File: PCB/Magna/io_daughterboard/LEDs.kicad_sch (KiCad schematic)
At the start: 90 parts, among them U2001 74HC595, U2002 74HC595, U2003 74HC595, U2004 74HC595, U2005 74HC595

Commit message: Split schematic to several projects
To allow for several boards to be done a kicad project
is needed for each
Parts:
- added TP2001, TP2002, TP2003, TP2004, TP2005, TP2006: TestPoint, TestPoint:TestPoint_Keystone_5005-5009_Compact, symbol Connector:TestPoint
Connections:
- net SPARE_LED6 is gone; now on net SPARE_LED5: D2038.1 (K), U2005.7 (QH)
- net CH1_0db: now also R2002.2; no longer D2002.1 (K)
- net CH1_12db: now also R2006.2; no longer D2006.1 (K)
- net CH1_20db: now also R2007.2; no longer D2007.1 (K)
- net CH1_25db: now also R2008.2; no longer D2008.1 (K)
- net CH1_3db: now also R2003.2; no longer D2003.1 (K)
- net CH1_6db: now also R2004.2; no longer D2004.1 (K)
- net CH1_9db: now also R2005.2; no longer D2005.1 (K)
- net CH1_clip: now also R2001.2; no longer D2001.1 (K)
- net CH2_0db: now also R2010.2; no longer D2010.1 (K)
- net CH2_12db: now also R2014.2; no longer D2014.1 (K)
- net CH2_20db: now also R2015.2; no longer D2015.1 (K)
- net CH2_25db: now also R2016.2; no longer D2016.1 (K)
- net CH2_3db: now also R2011.2; no longer D2011.1 (K)
- net CH2_6db: now also R2012.2; no longer D2012.1 (K)
- net CH2_9db: now also R2013.2; no longer D2013.1 (K)
- net CH2_clip: now also R2009.2; no longer D2009.1 (K)
- net GND: now also TP2003.1
- net MIDI_IN_INDICATOR: now also U2005.4 (QE); no longer U2005.3 (QD)
- net Master_0db: now also R2018.2; no longer D2018.1 (K)
- net Master_12db: now also R2022.2; no longer D2022.1 (K)
- net Master_20db: now also R2023.2; no longer D2023.1 (K)
- net Master_25db: now also R2024.2; no longer D2024.1 (K)
- net Master_3db: now also R2019.2; no longer D2019.1 (K)
- net Master_6db: now also R2020.2; no longer D2020.1 (K)
- net Master_9db: now also R2021.2; no longer D2021.1 (K)
- net Master_clip: now also R2017.2; no longer D2017.1 (K)
- net OE_output_ena: now also TP2005.1
- net OE_register__CLK: now also TP2002.1
- net OE_serial_CLK: now also TP2004.1
- net OE_serial_CLR: now also TP2001.1
- net OE_serial_in: now also TP2006.1
- net SPARE_LED2: now also D2039.1 (K); no longer D2037.1 (K)
- net SPARE_LED3: now also D2040.1 (K), U2005.5 (QF); no longer D2039.1 (K), U2005.4 (QE)
- net SPARE_LED4: now also D2036.1 (K), U2005.6 (QG); no longer D2040.1 (K), U2005.5 (QF)
- net SPARE_LED5: no longer D2036.1 (K), U2005.6 (QG)
- net VDD: now also D2001.2 (A), D2002.2 (A), D2003.2 (A), D2004.2 (A), D2005.2 (A), D2006.2 (A), D2007.2 (A), D2008.2 (A), D2009.2 (A), D2010.2 (A), D2011.2 (A), D2012.2 (A), D2013.2 (A), D2014.2 (A), D2015.2 (A), D2016.2 (A), D2017.2 (A), D2018.2 (A), D2019.2 (A), D2020.2 (A), D2021.2 (A), D2022.2 (A), D2023.2 (A), D2024.2 (A); no longer R2001.2, R2002.2, R2003.2, R2004.2, R2005.2, R2006.2, R2007.2, R2008.2, R2009.2, R2010.2, R2011.2, R2012.2, R2013.2, R2014.2, R2015.2, R2016.2, R2017.2, R2018.2, R2019.2, R2020.2, R2021.2, R2022.2, R2023.2, R2024.2
- net at R2002.1: now also D2002.1 (K); no longer D2002.2 (A)
- net at R2004.1: now also D2004.1 (K); no longer D2004.2 (A)
- net at R2015.1: now also D2015.1 (K); no longer D2015.2 (A)
- net at R2005.1: now also D2005.1 (K); no longer D2005.2 (A)
- net at R2014.1: now also D2014.1 (K); no longer D2014.2 (A)
- net at R2003.1: now also D2003.1 (K); no longer D2003.2 (A)
- net at R2022.1: now also D2022.1 (K); no longer D2022.2 (A)
- net at R2019.1: now also D2019.1 (K); no longer D2019.2 (A)
- net at R2007.1: now also D2007.1 (K); no longer D2007.2 (A)
- net at R2024.1: now also D2024.1 (K); no longer D2024.2 (A)
- net at R2020.1: now also D2020.1 (K); no longer D2020.2 (A)
- net at R2023.1: now also D2023.1 (K); no longer D2023.2 (A)
- net at R2010.1: now also D2010.1 (K); no longer D2010.2 (A)
- net at R2012.1: now also D2012.1 (K); no longer D2012.2 (A)
- net at R2001.1: now also D2001.1 (K); no longer D2001.2 (A)
- net at R2018.1: now also D2018.1 (K); no longer D2018.2 (A)
- net at R2009.1: now also D2009.1 (K); no longer D2009.2 (A)
- net at R2013.1: now also D2013.1 (K); no longer D2013.2 (A)
- net at R2006.1: now also D2006.1 (K); no longer D2006.2 (A)
- net at R2017.1: now also D2017.1 (K); no longer D2017.2 (A)
- net at R2016.1: now also D2016.1 (K); no longer D2016.2 (A)
- net at R2008.1: now also D2008.1 (K); no longer D2008.2 (A)
- net at R2011.1: now also D2011.1 (K); no longer D2011.2 (A)
- net at R2021.1: now also D2021.1 (K); no longer D2021.2 (A)
- new net EFFECT_CUE_STATUS: D2037.1 (K), U2005.3 (QD)
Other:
- moved on the sheet: D2001, D2002, D2003, D2004, D2005, D2006, D2007, D2008, D2009, D2010, D2011, D2012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

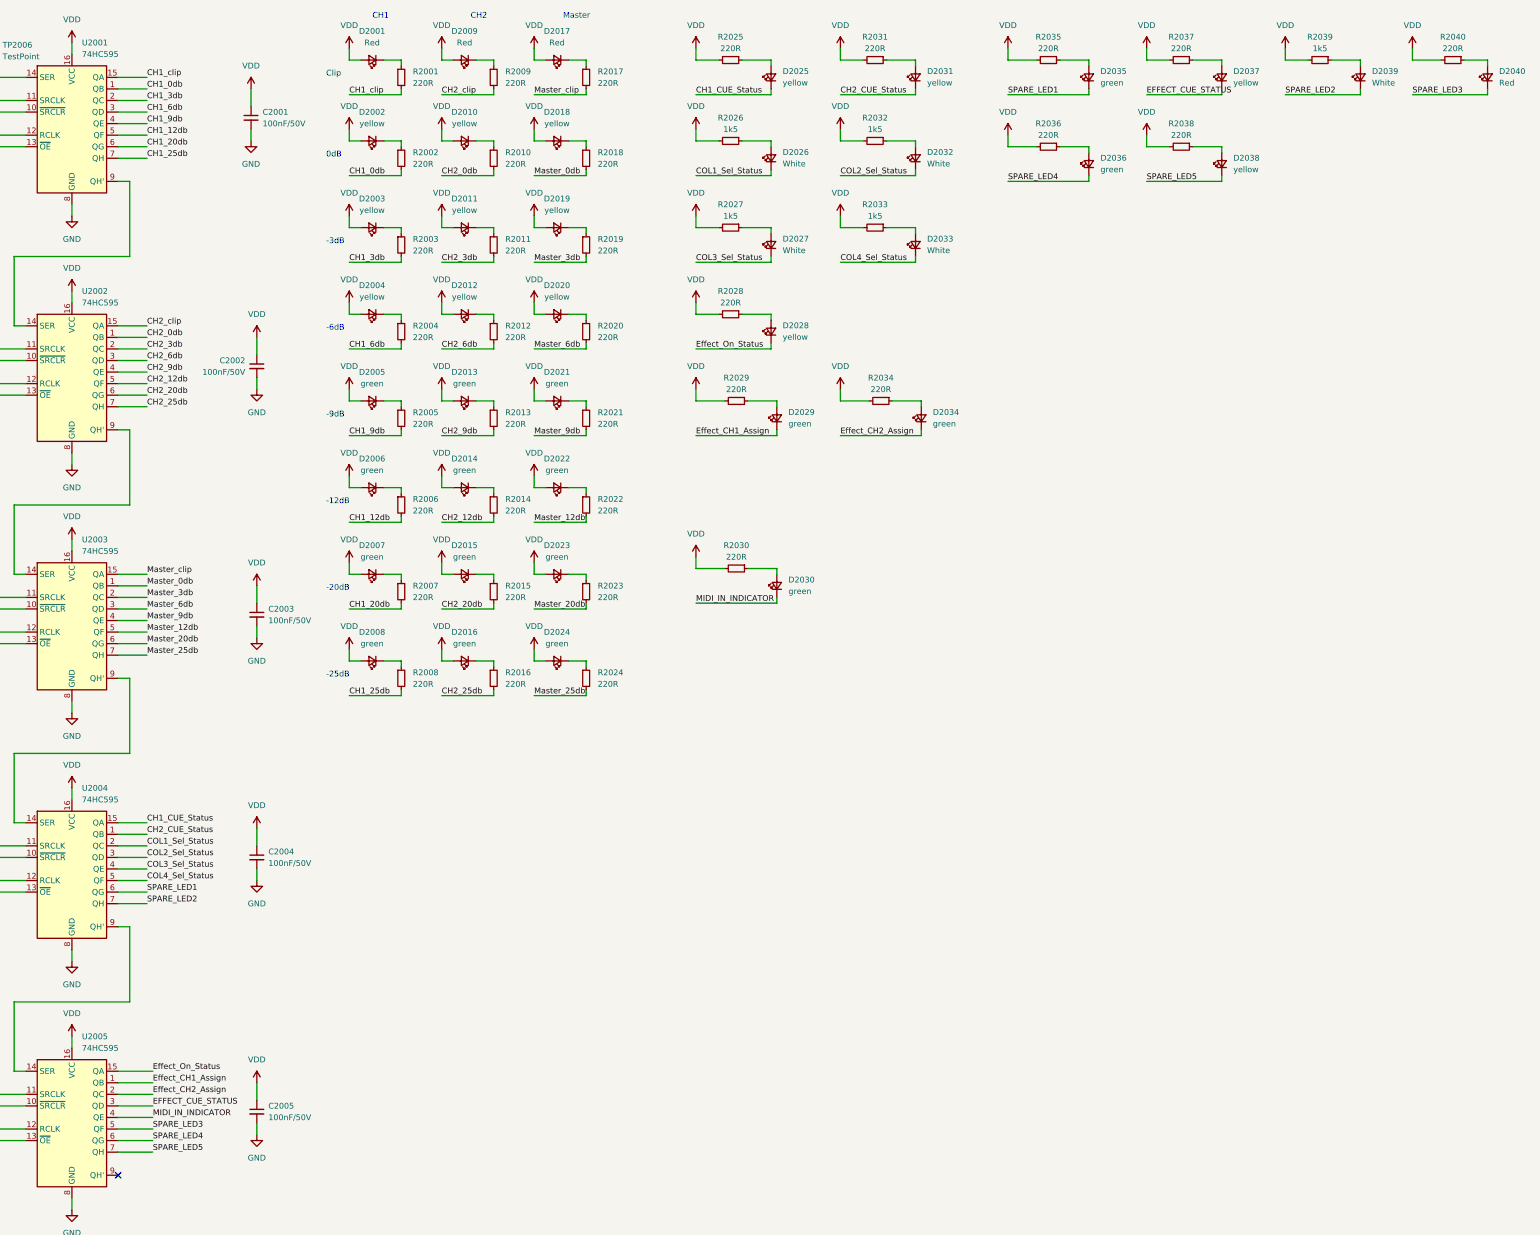
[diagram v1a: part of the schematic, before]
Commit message: Add a lot on the IO PCB
Also some schematic changes to accomodate issues found
when routing
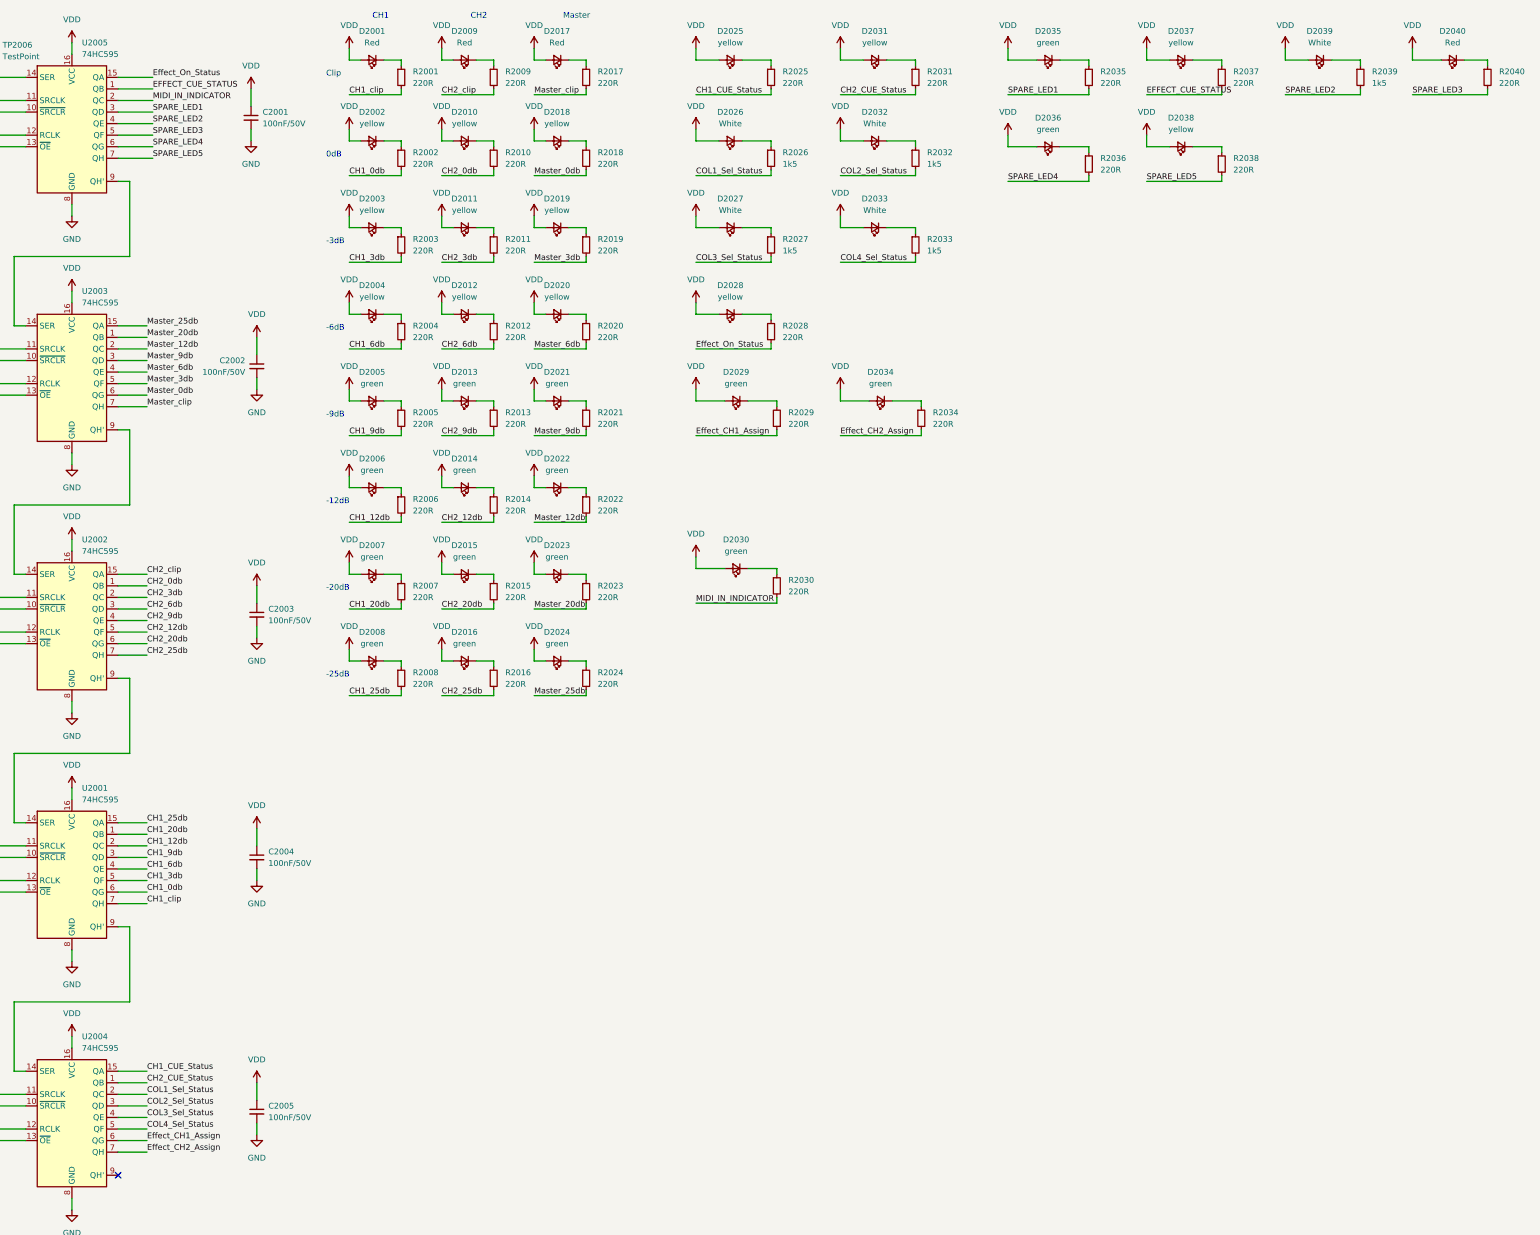
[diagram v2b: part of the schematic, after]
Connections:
- net CH1_0db: now also U2001.6 (QG); no longer U2001.1 (QB)
- net CH1_12db: now also U2001.2 (QC); no longer U2001.5 (QF)
- net CH1_20db: now also U2001.1 (QB); no longer U2001.6 (QG)
- net CH1_25db: now also U2001.15 (QA); no longer U2001.7 (QH)
- net CH1_3db: now also U2001.5 (QF); no longer U2001.2 (QC)
- net CH1_6db: now also U2001.4 (QE); no longer U2001.3 (QD)
- net CH1_9db: now also U2001.3 (QD); no longer U2001.4 (QE)
- net CH1_CUE_Status: now also R2025.2; no longer D2025.1 (K)
- net CH1_clip: now also U2001.7 (QH); no longer U2001.15 (QA)
- net CH2_CUE_Status: now also R2031.2; no longer D2031.1 (K)
- net COL1_Sel_Status: now also R2026.2; no longer D2026.1 (K)
- net COL2_Sel_Status: now also R2032.2; no longer D2032.1 (K)
- net COL3_Sel_Status: now also R2027.2; no longer D2027.1 (K)
- net COL4_Sel_Status: now also R2033.2; no longer D2033.1 (K)
- net EFFECT_CUE_STATUS: now also R2037.2, U2005.1 (QB); no longer D2037.1 (K), U2005.3 (QD)
- net Effect_CH1_Assign: now also R2029.1, U2004.6 (QG); no longer D2029.1 (K), U2005.1 (QB)
- net Effect_CH2_Assign: now also R2034.2, U2004.7 (QH); no longer D2034.1 (K), U2005.2 (QC)
- net Effect_On_Status: now also R2028.2; no longer D2028.1 (K)
- net MIDI_IN_INDICATOR: now also R2030.2, U2005.2 (QC); no longer D2030.1 (K), U2005.4 (QE)
- net Master_0db: now also U2003.6 (QG); no longer U2003.1 (QB)
- net Master_12db: now also U2003.2 (QC); no longer U2003.5 (QF)
- net Master_20db: now also U2003.1 (QB); no longer U2003.6 (QG)
- net Master_25db: now also U2003.15 (QA); no longer U2003.7 (QH)
- net Master_3db: now also U2003.5 (QF); no longer U2003.2 (QC)
- net Master_6db: now also U2003.4 (QE); no longer U2003.3 (QD)
- net Master_9db: now also U2003.3 (QD); no longer U2003.4 (QE)
- net Master_clip: now also U2003.7 (QH); no longer U2003.15 (QA)
- net OE_serial_in: now also U2005.14 (SER); no longer U2001.14 (SER)
- net SPARE_LED1: now also R2035.2, U2005.3 (QD); no longer D2035.1 (K), U2004.6 (QG)
- net SPARE_LED2: now also R2039.2, U2005.4 (QE); no longer D2039.1 (K), U2004.7 (QH)
- net SPARE_LED3: now also R2040.2; no longer D2040.1 (K)
- net SPARE_LED4: now also R2036.2; no longer D2036.1 (K)
- net SPARE_LED5: now also R2038.2; no longer D2038.1 (K)
- net VDD: now also D2025.2 (A), D2026.2 (A), D2027.2 (A), D2028.2 (A), D2029.2 (A), D2030.2 (A), D2031.2 (A), D2032.2 (A), D2033.2 (A), D2034.2 (A), D2035.2 (A), D2036.2 (A), D2037.2 (A), D2038.2 (A), D2039.2 (A), D2040.2 (A); no longer R2025.2, R2026.2, R2027.2, R2028.2, R2029.2, R2030.2, R2031.2, R2032.2, R2033.2, R2034.2, R2035.2, R2036.2, R2037.2, R2038.2, R2039.2, R2040.2
- net at R2036.1: now also D2036.1 (K); no longer D2036.2 (A)
- net at R2033.1: now also D2033.1 (K); no longer D2033.2 (A)
- net at R2039.1: now also D2039.1 (K); no longer D2039.2 (A)
- net at R2026.1: now also D2026.1 (K); no longer D2026.2 (A)
- net at R2031.1: now also D2031.1 (K); no longer D2031.2 (A)
- net at R2040.1: now also D2040.1 (K); no longer D2040.2 (A)
- net at R2027.1: now also D2027.1 (K); no longer D2027.2 (A)
- net at R2034.1: now also D2034.1 (K); no longer D2034.2 (A)
- net at U2002.14 (SER): now also U2003.9 (QH'); no longer U2001.9 (QH')
- net at U2002.9 (QH'): now also U2001.14 (SER); no longer U2003.14 (SER)
- net at R2032.1: now also D2032.1 (K); no longer D2032.2 (A)
- net at R2038.1: now also D2038.1 (K); no longer D2038.2 (A)
- net at R2035.1: now also D2035.1 (K); no longer D2035.2 (A)
- net at R2037.1: now also D2037.1 (K); no longer D2037.2 (A)
- net at U2004.9 (QH'): no longer U2005.14 (SER)
- net at U2005.9 (QH'): now also U2003.14 (SER)
- net at U2004.14 (SER): now also U2001.9 (QH'); no longer U2003.9 (QH')
- net at R2025.1: now also D2025.1 (K); no longer D2025.2 (A)
- net at R2030.1: now also D2030.1 (K); no longer D2030.2 (A)
- net at R2028.1: now also D2028.1 (K); no longer D2028.2 (A)
- new net: D2029.1 (K), R2029.2
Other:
- moved on the sheet: D2025, D2026, D2027, D2028, D2029, D2030, D2031, D2032, D2033, D2034, D2035, D2036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

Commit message: Route most of io daughterboard
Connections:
- net CH1_CUE_Status: now also U2004.2 (QC); no longer U2004.15 (QA)
- net CH1_clip: now also R2001.1; no longer R2001.2
- net COL1_Sel_Status: now also U2004.3 (QD); no longer U2004.2 (QC)
- net COL2_Sel_Status: now also U2004.4 (QE); no longer U2004.3 (QD)
- net COL3_Sel_Status: now also U2004.5 (QF); no longer U2004.4 (QE)
- net COL4_Sel_Status: now also U2004.6 (QG); no longer U2004.5 (QF)
- net EFFECT_CUE_STATUS: now also U2005.2 (QC); no longer U2005.1 (QB)
- net Effect_CH1_Assign: now also R2029.2, U2004.15 (QA); no longer R2029.1, U2004.6 (QG)
- net Effect_On_Status: now also U2005.1 (QB); no longer U2005.15 (QA)
- net GND: now also D2002.1 (K), D2003.1 (K), D2004.1 (K), D2005.1 (K), D2006.1 (K), D2007.1 (K), D2008.1 (K), D2009.1 (K), D2010.1 (K), D2011.1 (K), D2012.1 (K), D2013.1 (K), D2014.1 (K), D2015.1 (K), D2016.1 (K), D2017.1 (K), D2018.1 (K), D2019.1 (K), D2020.1 (K), D2021.1 (K), D2022.1 (K), D2023.1 (K), D2024.1 (K), D2025.1 (K), D2026.1 (K), D2027.1 (K), D2028.1 (K), D2029.1 (K), D2030.1 (K), D2031.1 (K), D2032.1 (K), D2033.1 (K), D2034.1 (K), D2035.1 (K), D2036.1 (K), D2037.1 (K), D2038.1 (K), D2039.1 (K), D2040.1 (K); no longer C2001.2
- net MIDI_IN_INDICATOR: now also R2030.1, U2005.15 (QA); no longer R2030.2, U2005.2 (QC)
- net SPARE_LED1: now also U2005.7 (QH); no longer U2005.3 (QD)
- net SPARE_LED2: now also U2005.6 (QG); no longer U2005.4 (QE)
- net SPARE_LED4: now also U2005.4 (QE); no longer U2005.6 (QG)
- net SPARE_LED5: now also U2005.3 (QD); no longer U2005.7 (QH)
- net VDD: no longer D2001.2 (A), D2002.2 (A), D2003.2 (A), D2004.2 (A), D2005.2 (A), D2006.2 (A), D2007.2 (A), D2008.2 (A), D2009.2 (A), D2010.2 (A), D2011.2 (A), D2012.2 (A), D2013.2 (A), D2014.2 (A), D2015.2 (A), D2016.2 (A), D2017.2 (A), D2018.2 (A), D2019.2 (A), D2020.2 (A), D2021.2 (A), D2022.2 (A), D2023.2 (A), D2024.2 (A), D2025.2 (A), D2026.2 (A), D2027.2 (A), D2028.2 (A), D2029.2 (A), D2030.2 (A), D2031.2 (A), D2032.2 (A), D2033.2 (A), D2034.2 (A), D2035.2 (A), D2036.2 (A), D2037.2 (A), D2038.2 (A), D2039.2 (A), D2040.2 (A)
- net at R2036.1: now also D2036.2 (A); no longer D2036.1 (K)
- net at R2002.1: now also D2002.2 (A); no longer D2002.1 (K)
- net at R2004.1: now also D2004.2 (A); no longer D2004.1 (K)
- net at R2033.1: now also D2033.2 (A); no longer D2033.1 (K)
- net at R2039.1: now also D2039.2 (A); no longer D2039.1 (K)
- net at R2015.1: now also D2015.2 (A); no longer D2015.1 (K)
- net at R2005.1: now also D2005.2 (A); no longer D2005.1 (K)
- net at R2014.1: now also D2014.2 (A); no longer D2014.1 (K)
- net at R2003.1: now also D2003.2 (A); no longer D2003.1 (K)
- net at R2022.1: now also D2022.2 (A); no longer D2022.1 (K)
- net at R2019.1: now also D2019.2 (A); no longer D2019.1 (K)
- net at R2026.1: now also D2026.2 (A); no longer D2026.1 (K)
- net at R2031.1: now also D2031.2 (A); no longer D2031.1 (K)
- net at R2007.1: now also D2007.2 (A); no longer D2007.1 (K)
- net at R2024.1: now also D2024.2 (A); no longer D2024.1 (K)
- net at R2040.1: now also D2040.2 (A); no longer D2040.1 (K)
- net at R2027.1: now also D2027.2 (A); no longer D2027.1 (K)
- net at R2034.1: now also D2034.2 (A); no longer D2034.1 (K)
- net at U2002.14 (SER): now also U2005.9 (QH'); no longer U2003.9 (QH')
- net at U2002.9 (QH'): now also U2003.14 (SER); no longer U2001.14 (SER)
- net at R2032.1: now also D2032.2 (A); no longer D2032.1 (K)
- net at R2038.1: now also D2038.2 (A); no longer D2038.1 (K)
- net at R2035.1: now also D2035.2 (A); no longer D2035.1 (K)
- net at R2020.1: now also D2020.2 (A); no longer D2020.1 (K)
- net at R2023.1: now also D2023.2 (A); no longer D2023.1 (K)
- net at R2010.1: now also D2010.2 (A); no longer D2010.1 (K)
- net at R2012.1: now also D2012.2 (A); no longer D2012.1 (K)
- net at R2037.1: now also D2037.2 (A); no longer D2037.1 (K)
- net at D2001.1 (K): no longer R2001.1
- net at R2025.1: now also D2025.2 (A); no longer D2025.1 (K)
- net at R2018.1: now also D2018.2 (A); no longer D2018.1 (K)
- net at R2009.1: now also D2009.2 (A); no longer D2009.1 (K)
- net at R2013.1: now also D2013.2 (A); no longer D2013.1 (K)
- net at R2006.1: now also D2006.2 (A); no longer D2006.1 (K)
- net at R2028.1: now also D2028.2 (A); no longer D2028.1 (K)
- net at R2017.1: now also D2017.2 (A); no longer D2017.1 (K)
- net at R2016.1: now also D2016.2 (A); no longer D2016.1 (K)
- net at R2008.1: now also D2008.2 (A); no longer D2008.1 (K)
- net at R2011.1: now also D2011.2 (A); no longer D2011.1 (K)
- net at R2021.1: now also D2021.2 (A); no longer D2021.1 (K)
- new net: D2001.2 (A), R2001.2
- new net: D2029.2 (A), R2029.1
- new net: U2001.14 (SER), U2003.9 (QH')
- new net: D2030.2 (A), R2030.2
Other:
- moved on the sheet: D2001, D2002, D2003, D2004, D2005, D2006, D2007, D2008, D2009, D2010, D2011, D2012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
